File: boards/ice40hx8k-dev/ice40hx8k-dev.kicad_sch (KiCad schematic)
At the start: 17 parts

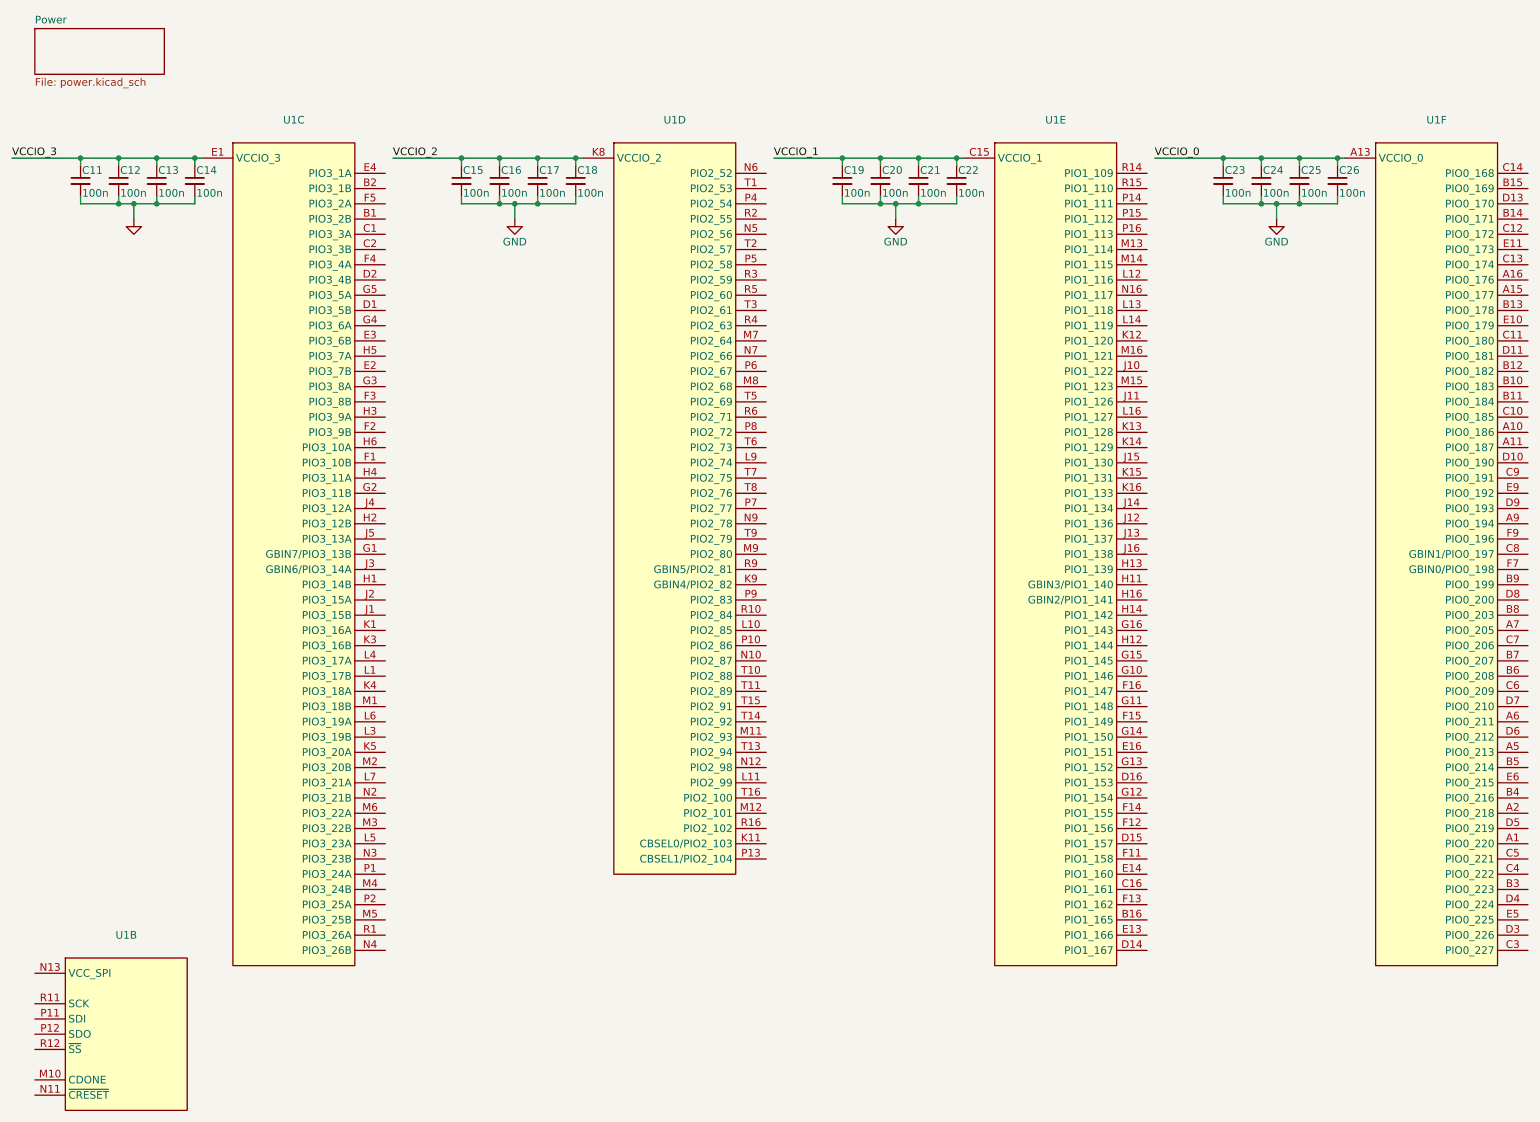
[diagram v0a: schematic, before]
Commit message: Split up schematic and label all nets.
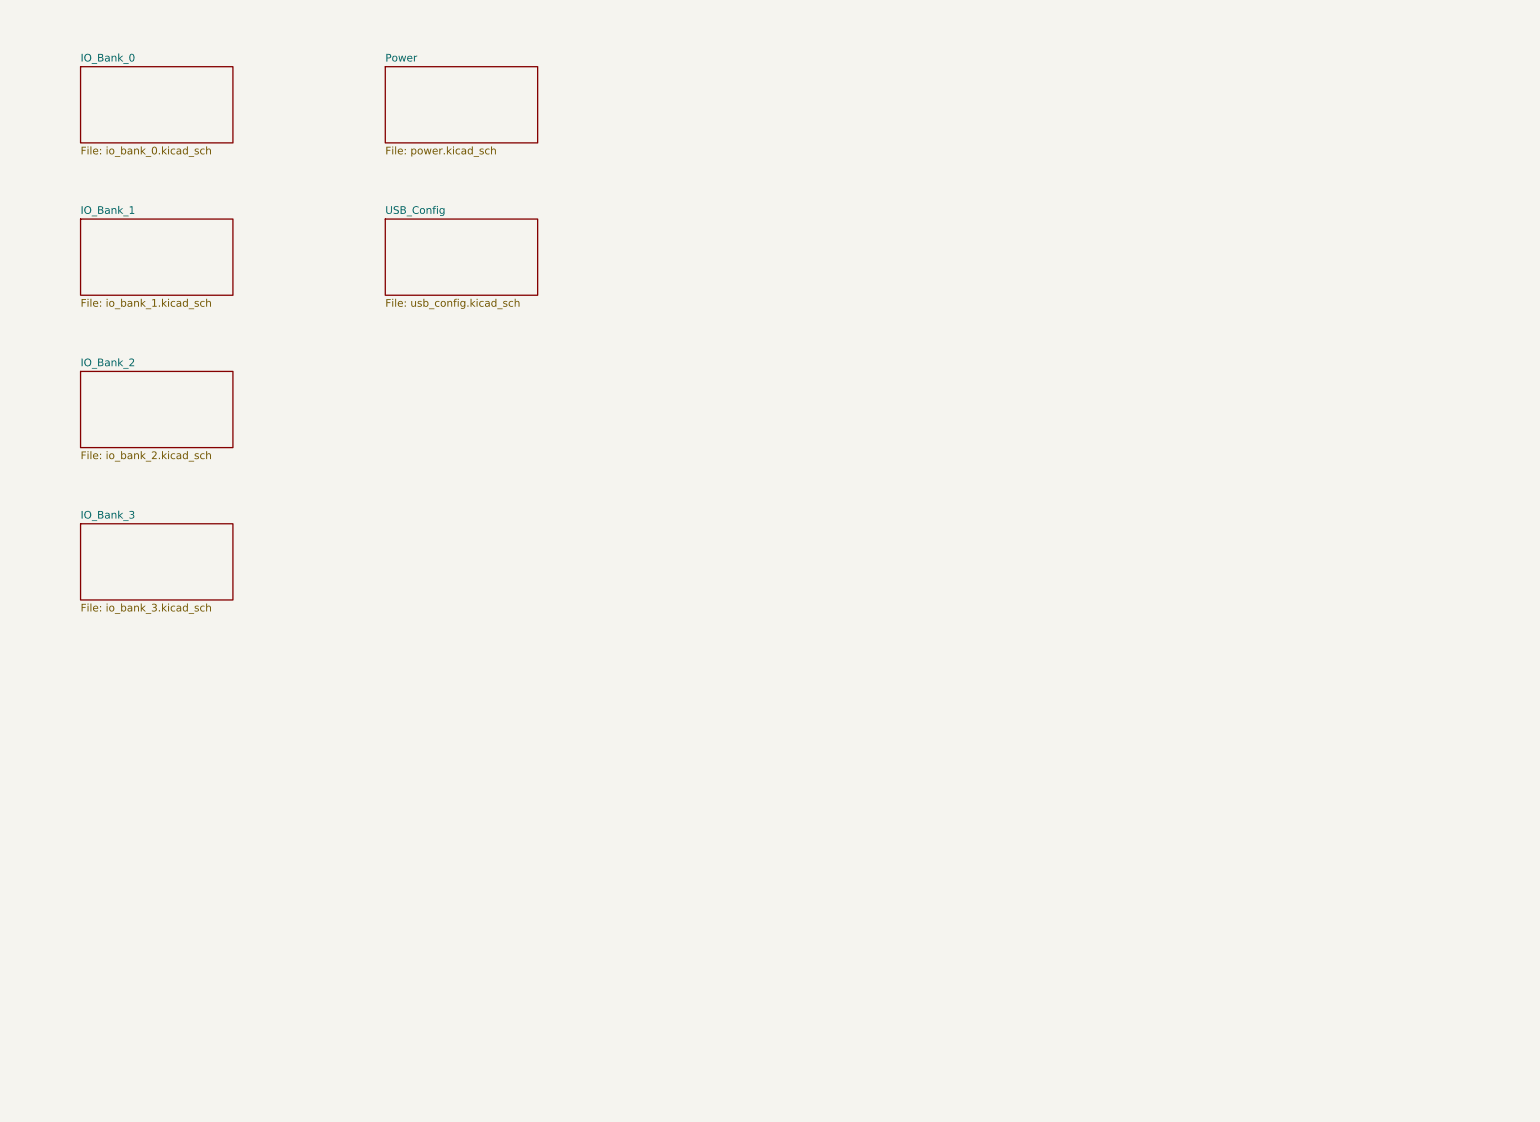
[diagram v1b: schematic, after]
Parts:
- removed C11, C12, C13, C14, C15, C16, C17, C18, C19, C20, C21, C22, C23, C24, C25, C26: 100n, 0Local:C_SMD_0402_Pad0.5mm, symbol Device:C_Small
- removed U1: (no value), symbol 0Local:ICE40HX8K-CT256
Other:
- added sheet IO_Bank_0 (io_bank_0.kicad_sch)
- added sheet IO_Bank_1 (io_bank_1.kicad_sch)
- added sheet IO_Bank_2 (io_bank_2.kicad_sch)
- added sheet IO_Bank_3 (io_bank_3.kicad_sch)
- added sheet USB_Config (usb_config.kicad_sch)
